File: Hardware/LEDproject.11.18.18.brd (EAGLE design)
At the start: 36.8 x 64.4 mm, 14 parts, among them IC1 ATMEGA328-PU, Y1 16MHz

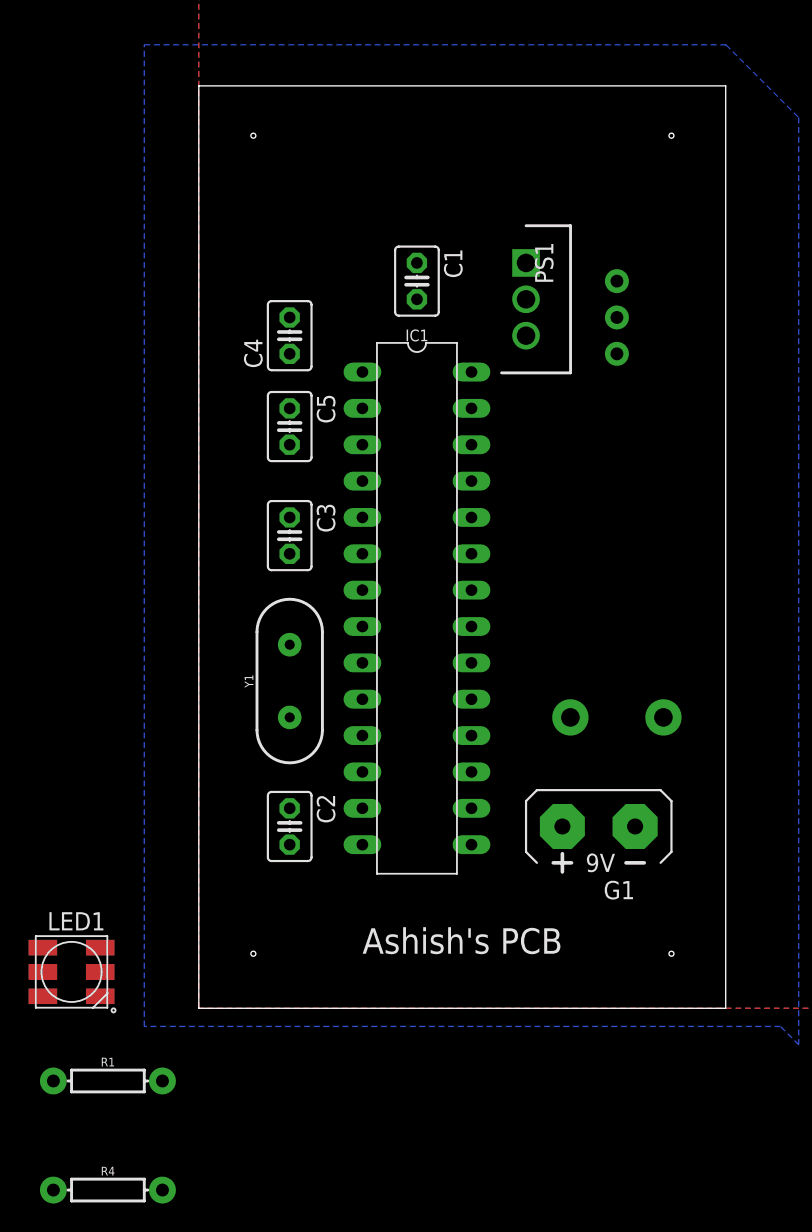
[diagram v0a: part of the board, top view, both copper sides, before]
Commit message: Changed LED to be surface mount
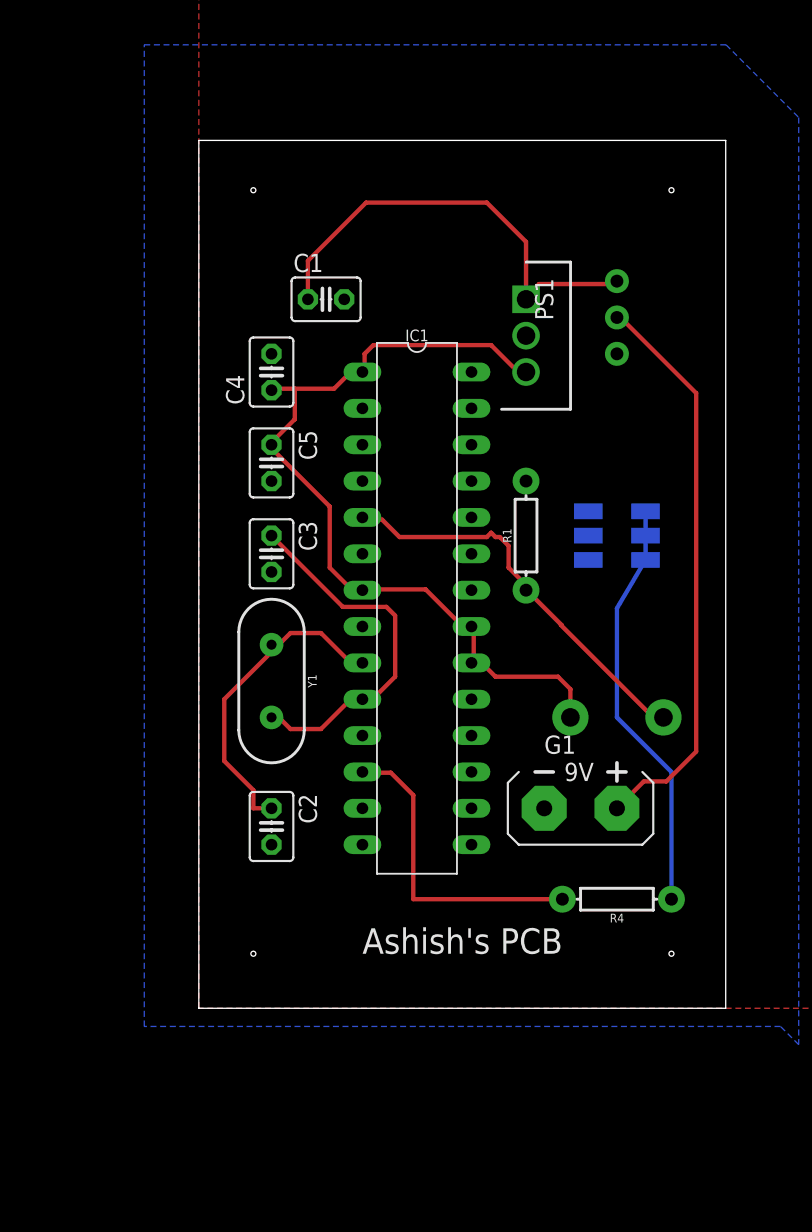
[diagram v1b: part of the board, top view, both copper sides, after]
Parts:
- moved LED1 48.8 mm to (29.2, 33.0), flipped to the bottom
- moved R1 48.0 mm to (22.9, 33.0), turned to 90 degrees
- moved R4 41.0 mm to (29.2, 7.62), turned to 180 degrees
- moved C1 6.48 mm to (8.89, 49.5), turned to 0 degrees
- moved C4 2.84 mm to (5.08, 44.5)
- moved C5 2.84 mm to (5.08, 38.1)
- moved PS1 2.54 mm to (22.9, 49.5)
- moved C3 1.80 mm to (5.08, 31.8)
- moved G1 1.80 mm to (26.7, 14.0), turned to 270 degrees
- moved C2 1.27 mm to (5.08, 12.7)
- moved Y1 1.27 mm to (5.08, 22.9), turned to 270 degrees
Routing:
- net +5V: track 0.00 -> 60.1 mm
- net N$3: track 0.00 -> 40.0 mm
- net N$5: track 0.00 -> 31.7 mm
- net N$4: track 0.00 -> 29.2 mm
- net N$6: track 0.00 -> 28.3 mm
- net N$2: track 0.00 -> 25.8 mm
- net N$1: track 0.00 -> 22.6 mm
- net N$7: track 0.00 -> 21.9 mm
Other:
- board size 36.8 x 64.4 mm -> 36.8 x 60.6 mm
